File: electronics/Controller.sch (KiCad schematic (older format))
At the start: 15 parts, among them IC1 Teensy++2.0, J1 Input 5v

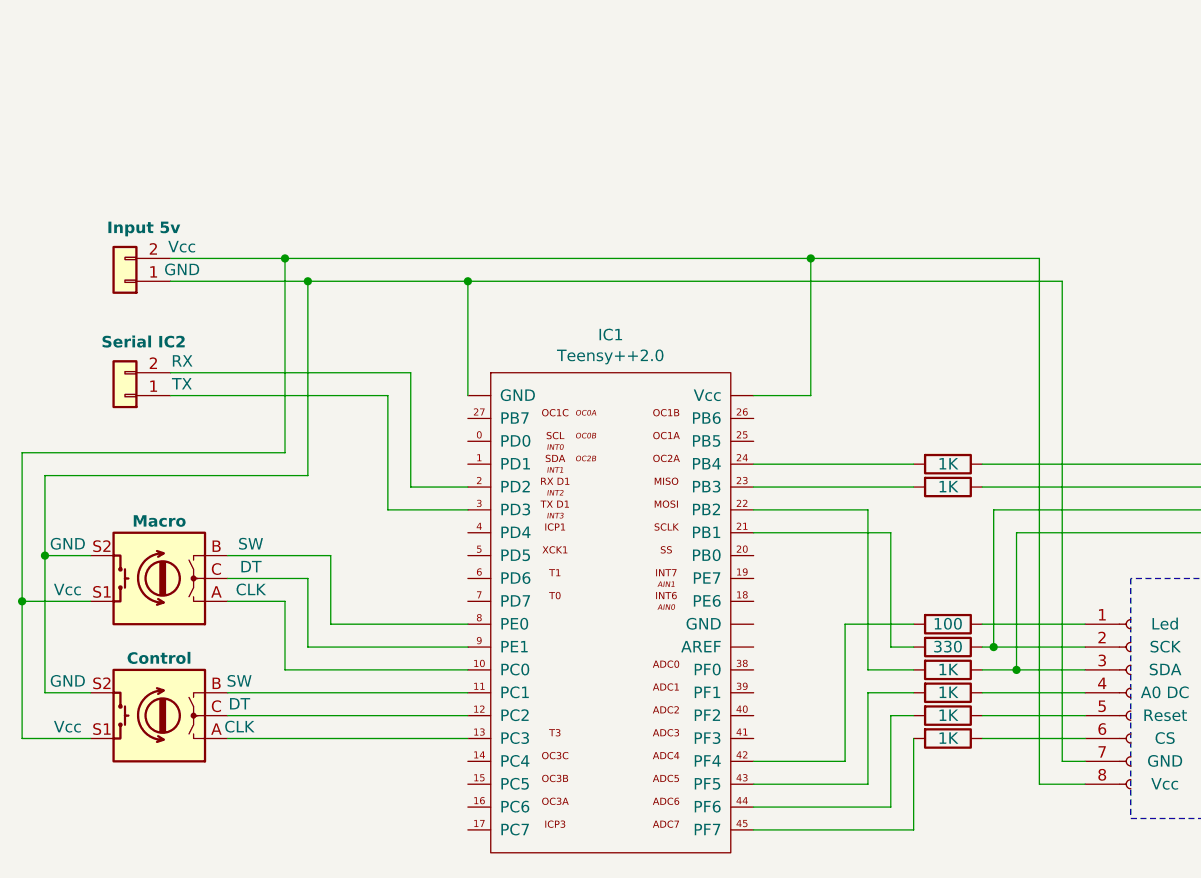
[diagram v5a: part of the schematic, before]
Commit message: Added PWM LED control
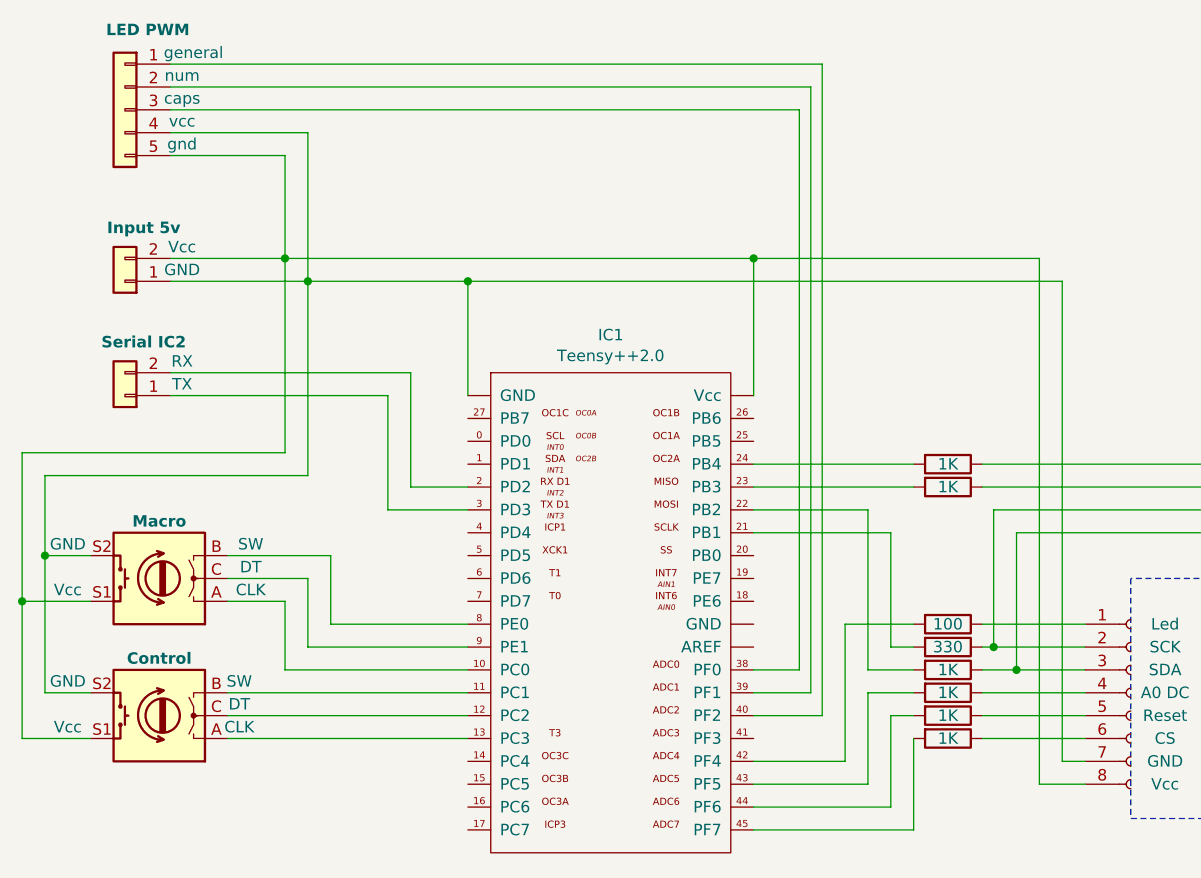
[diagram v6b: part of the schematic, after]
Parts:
- added J?: LED PWM, symbol Connector_Generic:Conn_01x05
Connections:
- net at Control.S2, IC1.~ (Vcc), J1.1 (Pin_1)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: now also J?.4 (Pin_4)
- net at Control.S1, IC1.~ (Vcc), J1.2 (Pin_2)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: now also J?.5 (Pin_5)
- net at IC1.38 (PF0): now also J?.3 (Pin_3)
- net at IC1.39 (PF1): now also J?.2 (Pin_2)
- net at IC1.40 (PF2): now also J?.1 (Pin_1)
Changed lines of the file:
@@
 Wire Wire Line
 	6400 4000 6600 4000
-Wire Wire Line
-	6150 2700 5900 2700
 $Comp
 L Device:Rotary_Encoder_Switch Control
@@
 	3350 2100 3850 2100
 Wire Wire Line
-	6150 2100 6150 2700
+	5900 2100 5900 2700
 $Comp
 L Device:Rotary_Encoder_Switch Macro
@@
 Connection ~ 3850 2100
 Wire Wire Line
-	3850 2100 6150 2100
+	3850 2100 5900 2100
 Wire Wire Line
 	7350 4400 7150 4400
 Wire Wire Line
 	7150 4400 7150 2100
-Connection ~ 6150 2100
+Connection ~ 5900 2100
 Wire Wire Line
 	4650 2200 4650 2700
@@
 	6300 3700 6600 3700
 Wire Wire Line
-	6150 2100 7150 2100
+	5900 2100 7150 2100
 Wire Wire Line
 	4650 2200 7250 2200
@@
 Wire Wire Line
 	4300 3200 4650 3200
+$Comp
+L Connector_Generic:Conn_01x05 J?
+U 1 1 5F2EB678
+P 3150 1450
+F 0 "J?" H 3068 1867 50  0001 C CNN
+F 1 "LED PWM" H 3050 1800 50  0000 C CNB
+F 2 "" H 3150 1450 50  0001 C CNN
+F 3 "~" H 3150 1450 50  0001 C CNN
+F 4 "vcc" H 2900 1400 50  0000 C CNN "vcc"
+F 5 "gnd" H 2900 1300 50  0000 C CNN "gnd"
+F 6 "general" H 2850 1700 50  0000 C CNN "general"
+F 7 "num" H 2900 1600 50  0000 C CNN "num"
+F 8 "caps" H 2900 1500 50  0000 C CNN "caps"
+	1    3150 1450
+	-1   0    0    -1
+$EndComp
+Wire Wire Line
+	3850 2100 3850 1650
+Wire Wire Line
+	3850 1650 3350 1650
+Wire Wire Line
+	3950 2200 3950 1550
+Wire Wire Line
+	3950 1550 3350 1550
+Wire Wire Line
+	5900 4100 6200 4100
+Wire Wire Line
+	6200 4100 6200 1250
+Wire Wire Line
+	6200 1250 3350 1250
+Wire Wire Line
+	5900 4000 6150 4000
+Wire Wire Line
+	6150 4000 6150 1350
+Wire Wire Line
+	6150 1350 3350 1350
+Wire Wire Line
+	5900 3900 6100 3900
+Wire Wire Line
+	6100 3900 6100 1450
+Wire Wire Line
+	6100 1450 3350 1450
 $EndSCHEMATC

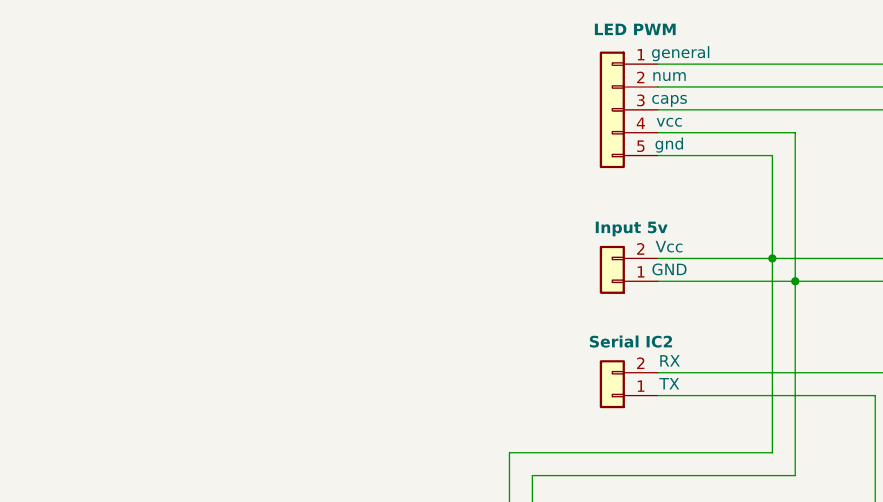
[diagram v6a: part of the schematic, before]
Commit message: IRF 520 Power for keybd backlight
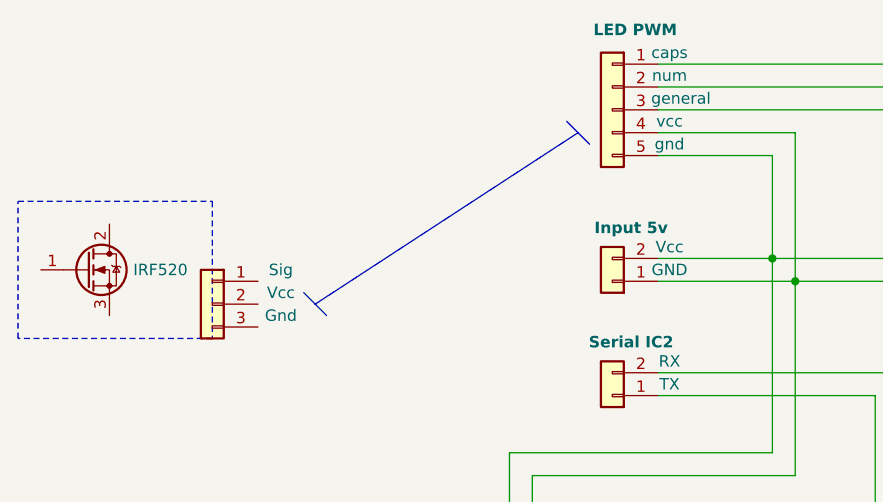
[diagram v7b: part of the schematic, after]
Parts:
- added J?: IRF 520, symbol Connector_Generic:Conn_01x03
- added Q?: IRF520, Package_TO_SOT_THT:TO-220-3_Vertical, symbol Transistor_FET:IRF540N
- J?: general general -> general
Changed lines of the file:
@@
 F 4 "vcc" H 2900 1400 50  0000 C CNN "vcc"
 F 5 "gnd" H 2900 1300 50  0000 C CNN "gnd"
-F 6 "general" H 2850 1700 50  0000 C CNN "general"
+F 6 " general" H 2850 1500 50  0000 C CNN "general"
 F 7 "num" H 2900 1600 50  0000 C CNN "num"
-F 8 "caps" H 2900 1500 50  0000 C CNN "caps"
+F 8 "caps" H 2900 1700 50  0000 C CNN "caps"
 	1    3150 1450
 	-1   0    0    -1
@@
 Wire Wire Line
 	6100 1450 3350 1450
+$Comp
+L Transistor_FET:IRF540N Q?
+U 1 1 5F304FB3
+P 850 2150
+F 0 "Q?" H 1054 2196 50  0001 L CNN
+F 1 "IRF520" H 1054 2150 50  0000 L CNN
+F 2 "Package_TO_SOT_THT:TO-220-3_Vertical" H 1100 2075 50  0001 L CIN
+F 3 "http://www.irf.com/product-info/datasheets/data/irf540n.pdf" H 850 2150 50  0001 L CNN
+	1    850  2150
+	1    0    0    -1
+$EndComp
+Wire Notes Line style solid rgb(255, 0, 0)
+	550  1850 1400 1850
+Wire Notes Line style solid rgb(255, 0, 0)
+	1400 1850 1400 2450
+Wire Notes Line style solid rgb(255, 0, 0)
+	1400 2450 550  2450
+Wire Notes Line style solid rgb(255, 0, 0)
+	550  2450 550  1850
+$Comp
+L Connector_Generic:Conn_01x03 J?
+U 1 1 5F32334A
+P 1400 2300
+F 0 "J?" H 1480 2342 50  0001 L CNN
+F 1 "IRF 520" H 1650 2350 50  0001 C CNN
+F 2 "" H 1400 2300 50  0001 C CNN
+F 3 "~" H 1400 2300 50  0001 C CNN
+F 4 "Sig" H 1100 2450 50  0000 C CNN "SIG"
+F 5 "Vcc" H 1100 2350 50  0000 C CNN "Vcc"
+F 6 "Gnd" H 1100 2250 50  0000 C CNN "Gnd"
+	1    1400 2300
+	-1   0    0    -1
+$EndComp
+Wire Bus Line
+	1850 2300 3000 1550
+Entry Bus Bus
+	1800 2250 1900 2350
+Entry Bus Bus
+	2950 1500 3050 1600
 $EndSCHEMATC

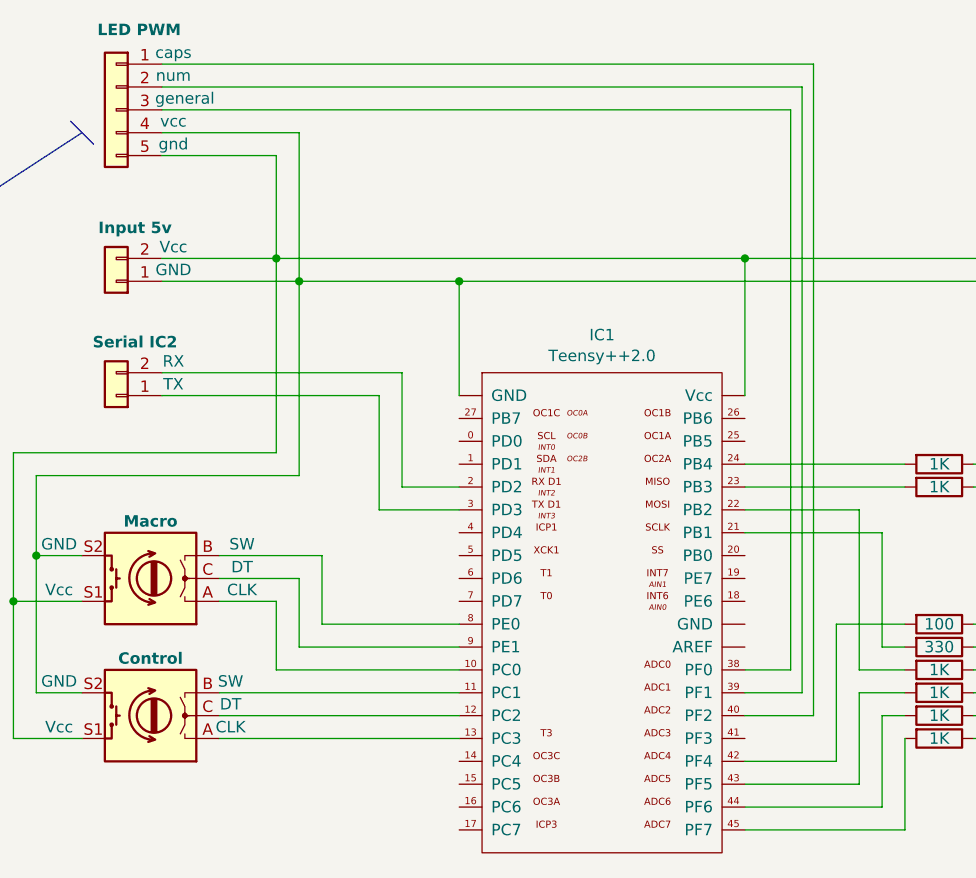
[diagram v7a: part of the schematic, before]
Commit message: Using PVM outputs for backlight leds
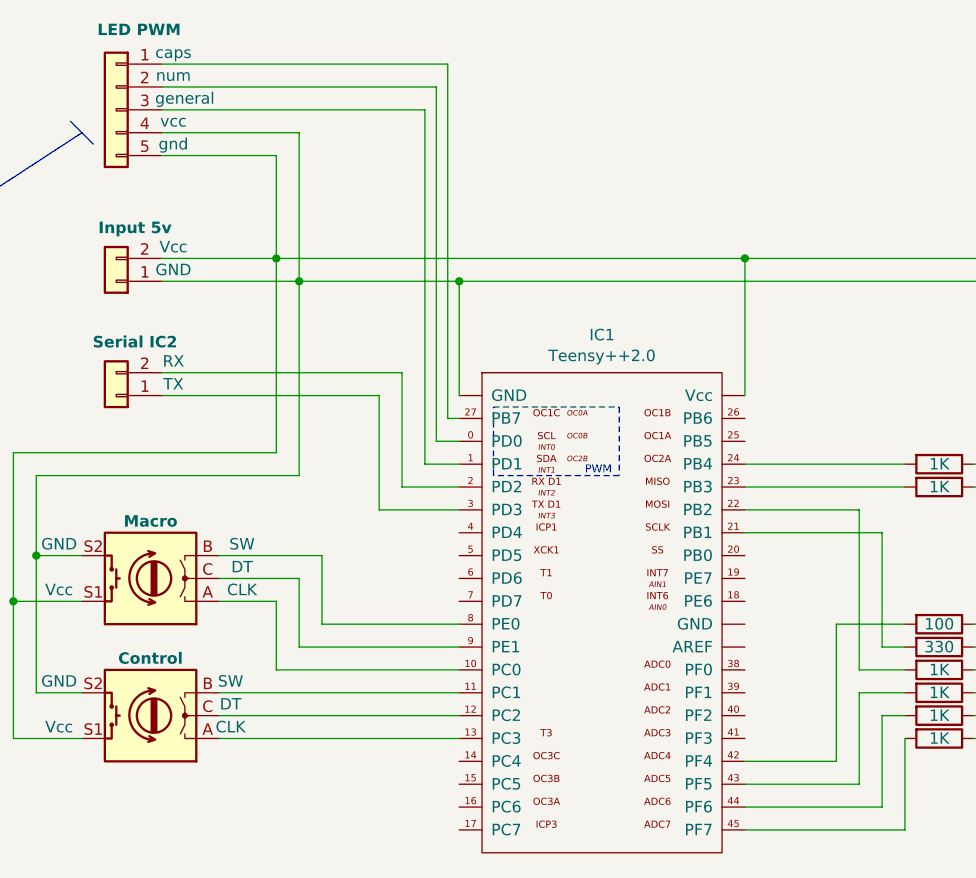
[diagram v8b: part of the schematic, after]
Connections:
- net at IC1.0 (PD0): now also J?.2 (Pin_2)
- net at IC1.1 (PD1): now also J?.3 (Pin_3)
- net at IC1.27 (PB7): now also J?.1 (Pin_1)
- net at IC1.38 (PF0): no longer J?.3 (Pin_3)
- net at IC1.39 (PF1): no longer J?.2 (Pin_2)
- net at IC1.40 (PF2): no longer J?.1 (Pin_1)
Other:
- note added: "PWM"
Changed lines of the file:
@@
 Wire Wire Line
 	3950 1550 3350 1550
-Wire Wire Line
-	5900 4100 6200 4100
-Wire Wire Line
-	6200 4100 6200 1250
-Wire Wire Line
-	6200 1250 3350 1250
-Wire Wire Line
-	5900 4000 6150 4000
-Wire Wire Line
-	6150 4000 6150 1350
-Wire Wire Line
-	6150 1350 3350 1350
-Wire Wire Line
-	5900 3900 6100 3900
-Wire Wire Line
-	6100 3900 6100 1450
-Wire Wire Line
-	6100 1450 3350 1450
 $Comp
 L Transistor_FET:IRF540N Q?
@@
 Entry Bus Bus
 	2950 1500 3050 1600
+Wire Wire Line
+	4600 2800 4650 2800
+Wire Wire Line
+	4550 2900 4650 2900
+Wire Wire Line
+	4500 3000 4650 3000
+Wire Wire Line
+	4500 1450 4500 3000
+Wire Wire Line
+	4500 1450 3350 1450
+Wire Wire Line
+	4550 1350 3350 1350
+Wire Wire Line
+	4550 2900 4550 1350
+Wire Wire Line
+	4600 1250 3350 1250
+Wire Wire Line
+	4600 2800 4600 1250
+Wire Notes Line
+	4800 3050 4800 2750
+Wire Notes Line
+	4800 2750 5350 2750
+Wire Notes Line
+	5350 2750 5350 3050
+Wire Notes Line
+	5350 3050 4800 3050
+Text Notes 5200 3050 0    35   ~ 0
+PWM
 $EndSCHEMATC
